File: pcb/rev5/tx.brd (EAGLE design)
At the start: 28 x 36.5 mm, 55 parts, among them IC1 STM32F030F4, IC2 NRF24L01ALT1, Q1 BSS84, SW2 324_SW324_SWITCH_FOOT_HOLE, U2 USBC_16P, U3 MCP73831T-2ACI/OT, U4 XC6206_DEV, Y1 16MHz_12pF

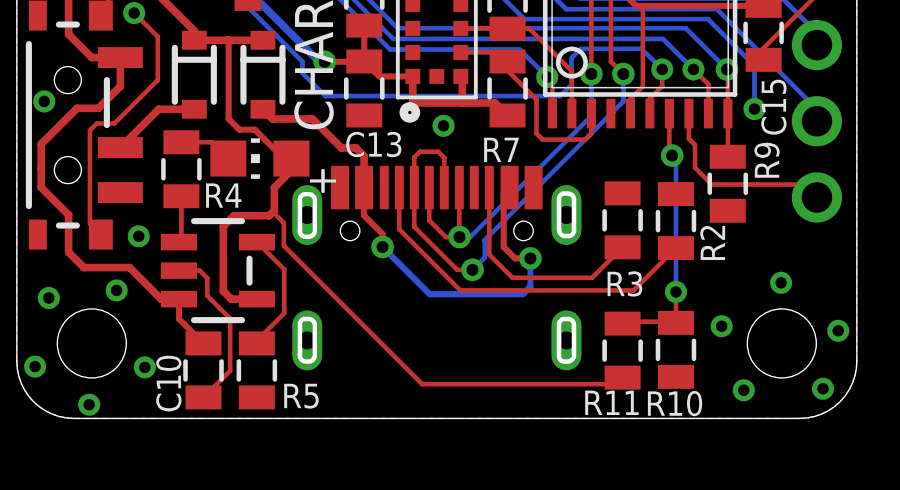
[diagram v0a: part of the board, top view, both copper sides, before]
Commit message: added trig_out on RX, preparing for next production run
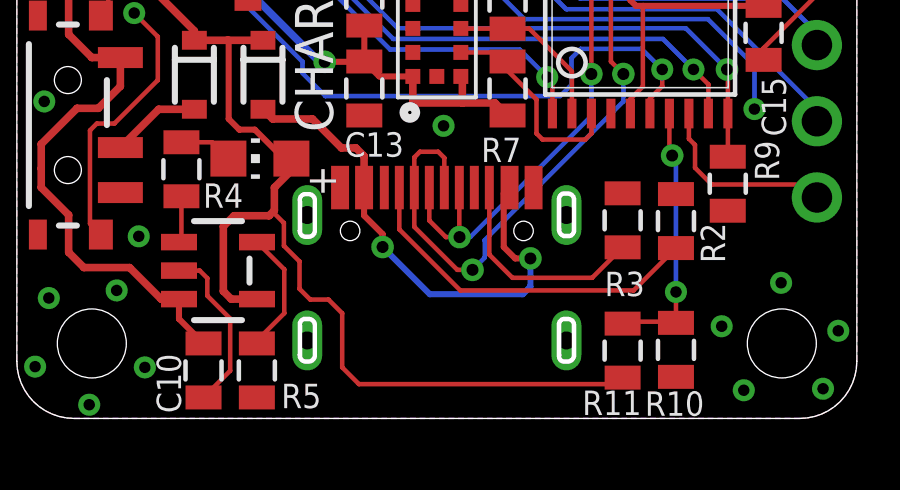
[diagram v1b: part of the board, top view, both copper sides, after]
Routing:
- net N$27: track 34.3 -> 35.9 mm
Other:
- board text added: "PD2 190823"
- board text removed: "PD3 191005"
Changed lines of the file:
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@@
 <text x="14" y="31.017" size="1.27" layer="26" font="vector" rot="MR0" align="center">dekuNukem 2019</text>
 <text x="14" y="33.205" size="1.524" layer="26" rot="MR0" align="center">git.io/daytripper</text>
-<text x="14" y="2.7432" size="1.27" layer="26" rot="MR0" align="center">PD3
-191005</text>
+<text x="14" y="2.7432" size="1.27" layer="26" rot="MR0" align="center">PD2
+190823</text>
 <text x="1.6256" y="13.9192" size="1.27" layer="26" rot="MR270">ON</text>
 <text x="1.6256" y="7.366" size="1.27" layer="26" rot="MR270">OFF</text>
@@
 <wire x1="8.4074" y1="6.7564" x2="7.239" y2="6.7564" width="0.254" layer="1"/>
 <wire x1="6.8834" y1="4.2418" x2="6.8834" y2="6.4008" width="0.254" layer="1"/>
+<wire x1="9.4234" y1="5.2324" x2="8.9027" y2="5.7531" width="0.1524" layer="1"/>
 <wire x1="20.193" y1="1.3606" x2="19.9754" y2="1.143" width="0.1524" layer="1"/>
-<wire x1="19.9754" y1="1.143" x2="13.5128" y2="1.143" width="0.1524" layer="1"/>
-<wire x1="13.5128" y1="1.143" x2="8.9027" y2="5.7531" width="0.1524" layer="1"/>
+<wire x1="19.9754" y1="1.143" x2="11.4046" y2="1.143" width="0.1524" layer="1"/>
+<wire x1="11.4046" y1="1.143" x2="10.8458" y2="1.7018" width="0.1524" layer="1"/>
+<wire x1="10.8458" y1="1.7018" x2="10.8458" y2="3.5052" width="0.1524" layer="1"/>
+<wire x1="10.8458" y1="3.5052" x2="10.3886" y2="3.9624" width="0.1524" layer="1"/>
+<wire x1="10.3886" y1="3.9624" x2="9.779" y2="3.9624" width="0.1524" layer="1"/>
+<wire x1="9.779" y1="3.9624" x2="9.4234" y2="4.318" width="0.1524" layer="1"/>
+<wire x1="9.4234" y1="4.318" x2="9.4234" y2="5.2324" width="0.1524" layer="1"/>
 <wire x1="9.1526" y1="8.6614" x2="9.1526" y2="8.2636" width="0.254" layer="1"/>
 <wire x1="9.1526" y1="8.2636" x2="8.5852" y2="7.6962" width="0.254" layer="1"/>
